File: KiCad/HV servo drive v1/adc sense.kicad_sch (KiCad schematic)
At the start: 38 parts, among them J6 PFC SENSE

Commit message: KiCad 8.0 update
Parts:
- renumbered C36 to C28, C28 to C29, C29 to C30, C30 to C33, C33 to C34, C34 to C35, C35 to C36, D9 to D10, D10 to D12, D12 to D13, D13 to D14, D14 to D15, D15 to D8, D8 to D9, R44 to R25, R45 to R26, R25 to R27, R26 to R28, R27 to R29, R28 to R30, R29 to R38, R30 to R39, R38 to R40, R39 to R41, R40 to R42, R41 to R43, R42 to R44, R43 to R45

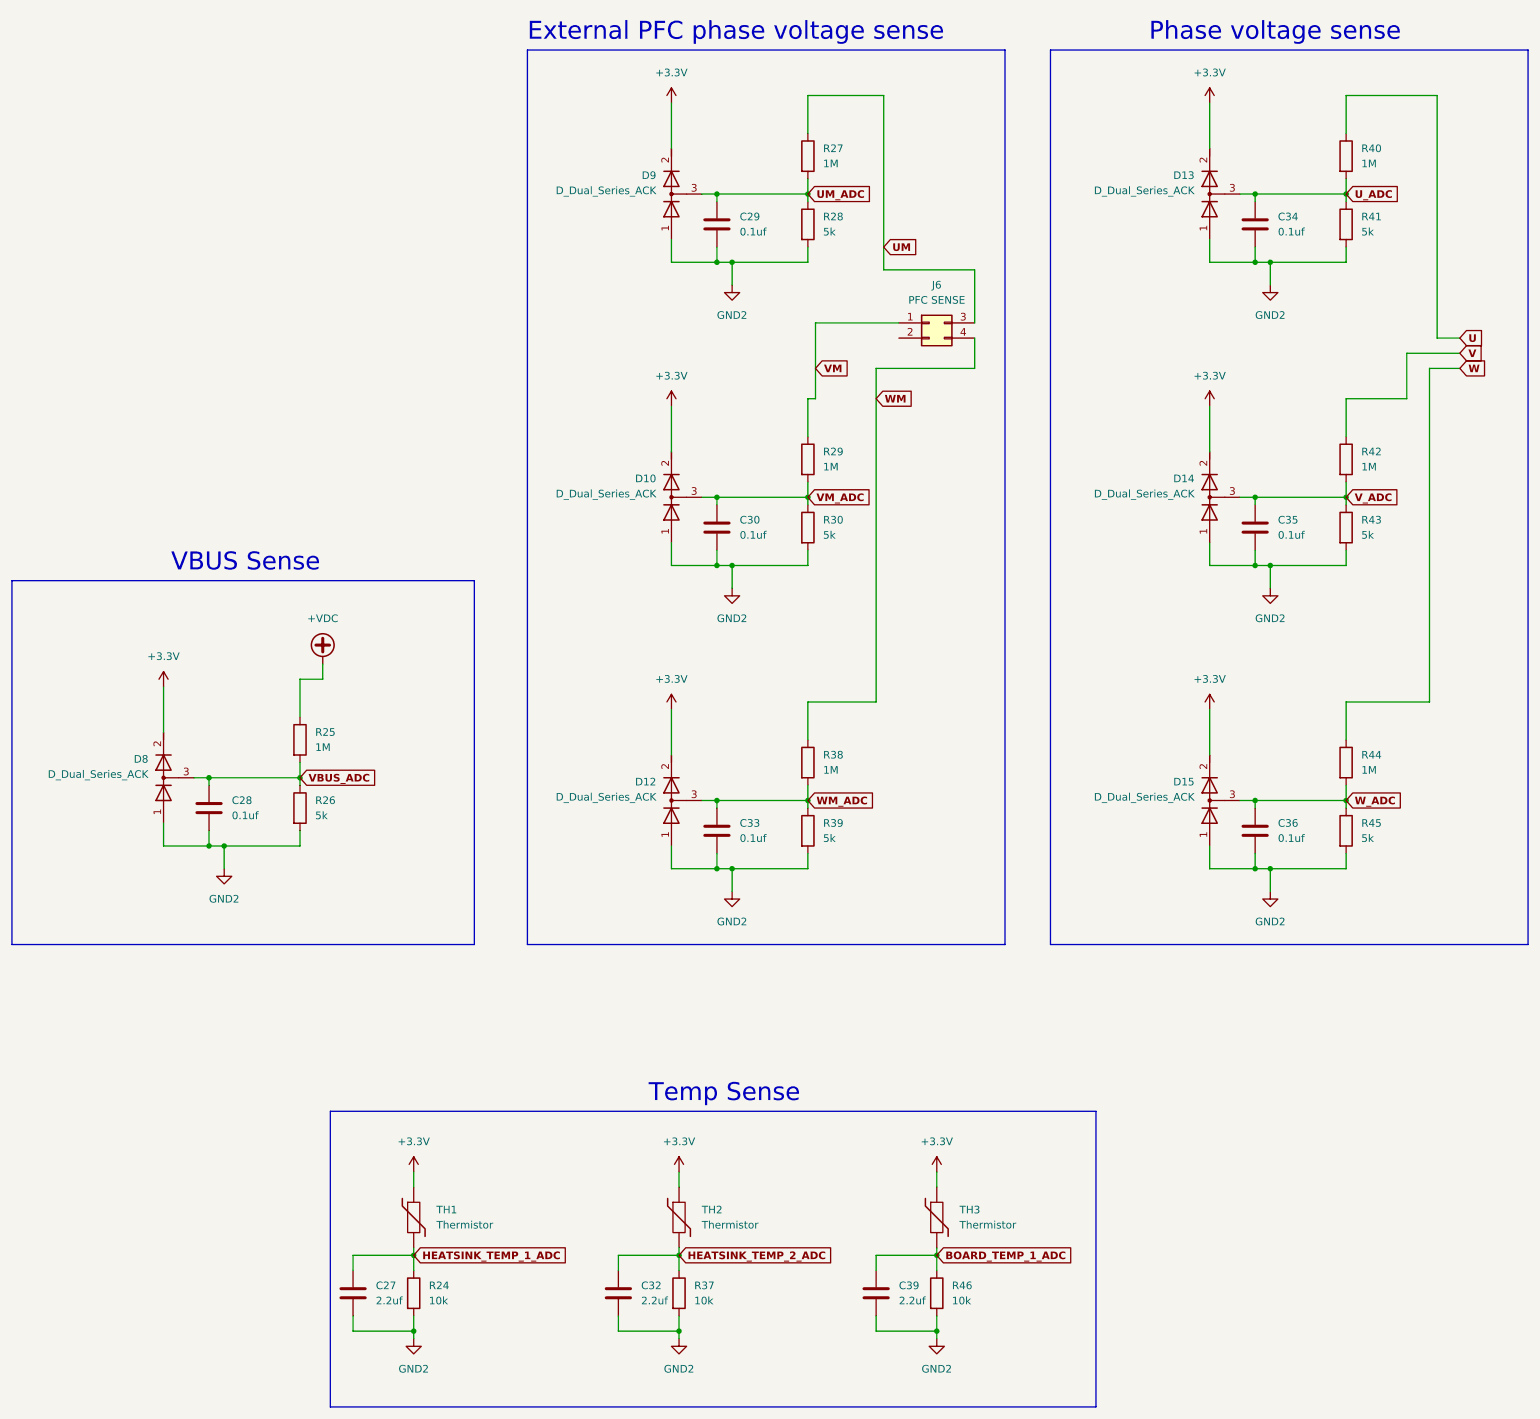
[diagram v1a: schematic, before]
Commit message: start rev 2 changes
fix component references, fix rj45 and dc-dc converter footprints, add RLC filters on all power connectors, add more mounting holes
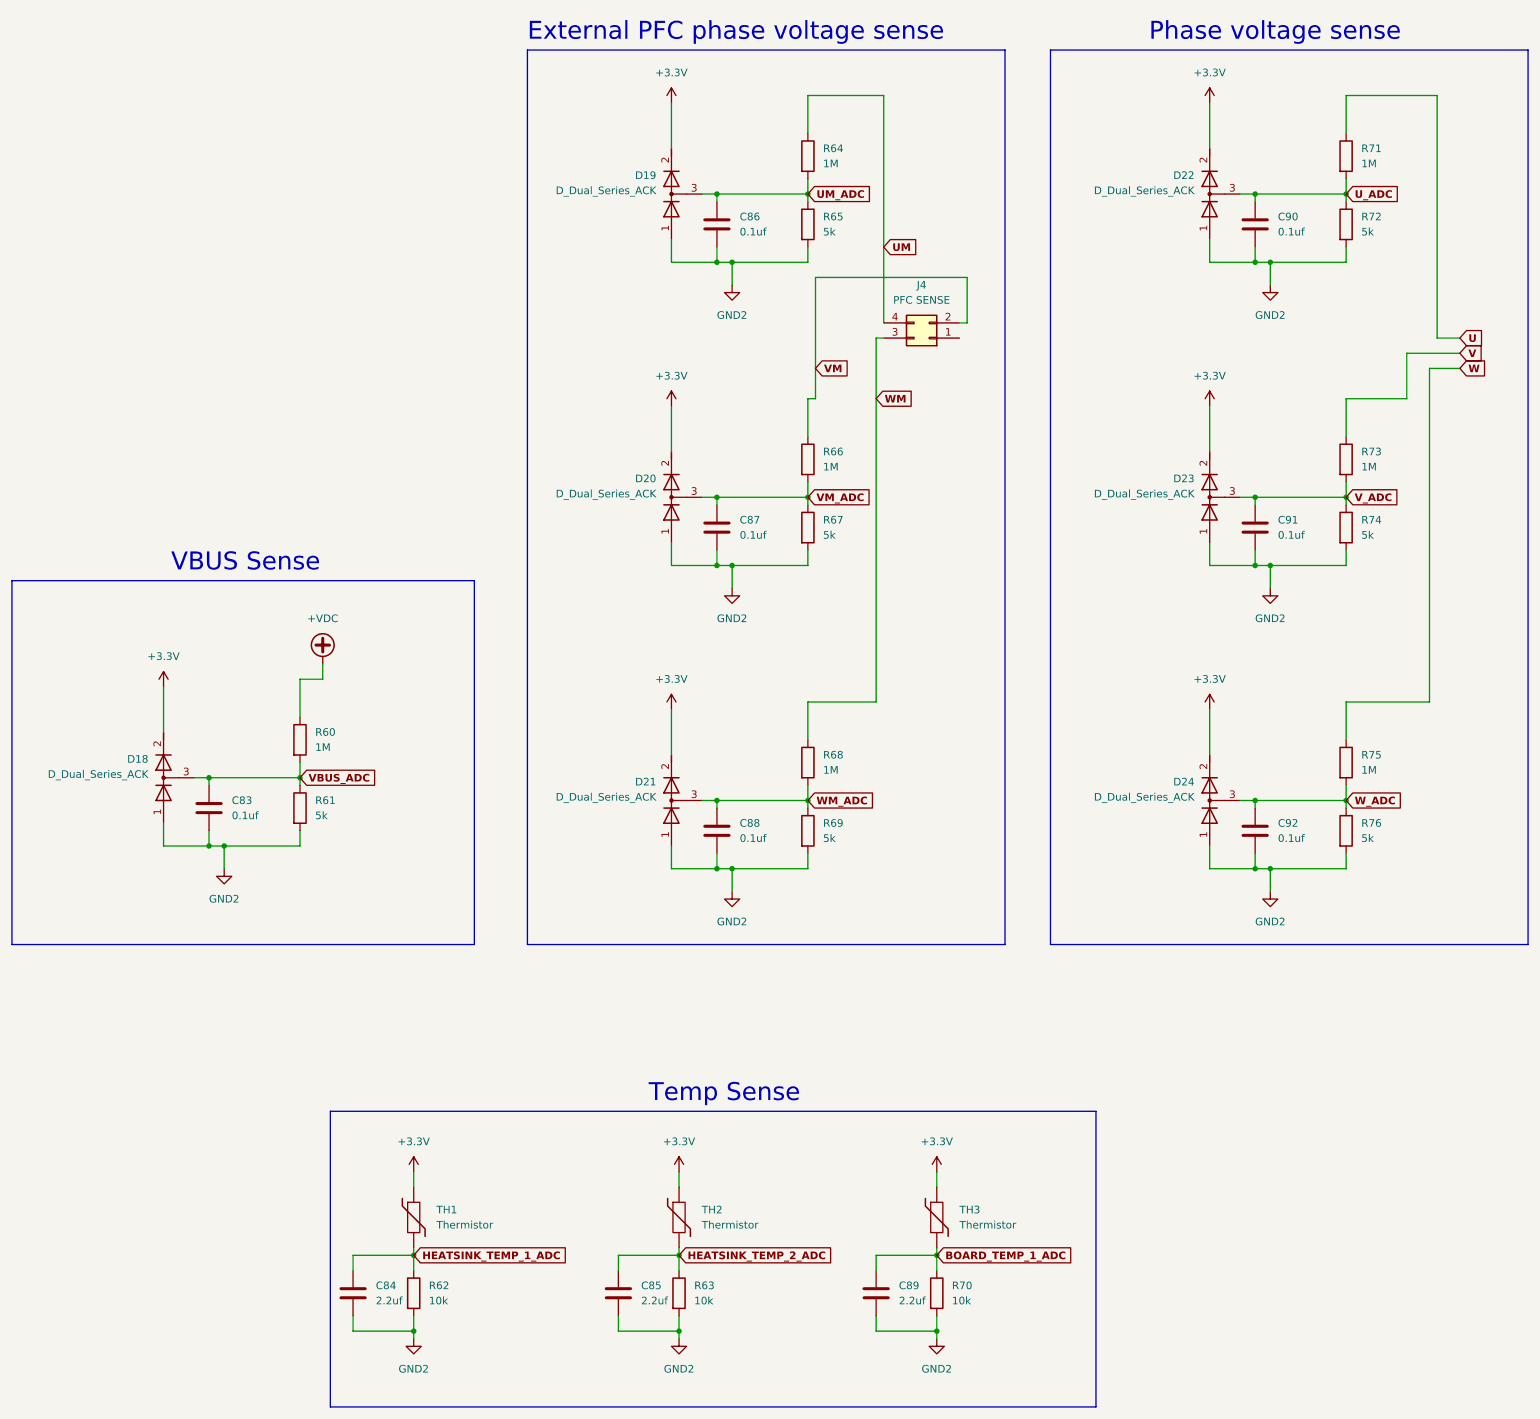
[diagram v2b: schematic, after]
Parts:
- renumbered C28 to C83, C27 to C84, C32 to C85, C29 to C86, C30 to C87, C33 to C88, C39 to C89, C34 to C90, C35 to C91, C36 to C92, D8 to D18, D9 to D19, D10 to D20, D12 to D21, D13 to D22, D14 to D23, D15 to D24, J6 to J4, R25 to R60, R26 to R61, R24 to R62, R37 to R63, R27 to R64, R28 to R65, R29 to R66, R30 to R67, R38 to R68, R39 to R69, R46 to R70, R40 to R71, R41 to R72, R42 to R73, R43 to R74, R44 to R75, R45 to R76
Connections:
- net UM: now also J4.4 (Pin_4); no longer J4.3 (Pin_3)
- net VM: now also J4.2 (Pin_2); no longer J4.1 (Pin_1)
- net WM: now also J4.3 (Pin_3); no longer J4.4 (Pin_4)
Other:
- moved on the sheet: J4

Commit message: update to rev 2.1
basically the same version as in the FOC youtube video, with some minor issues fixed
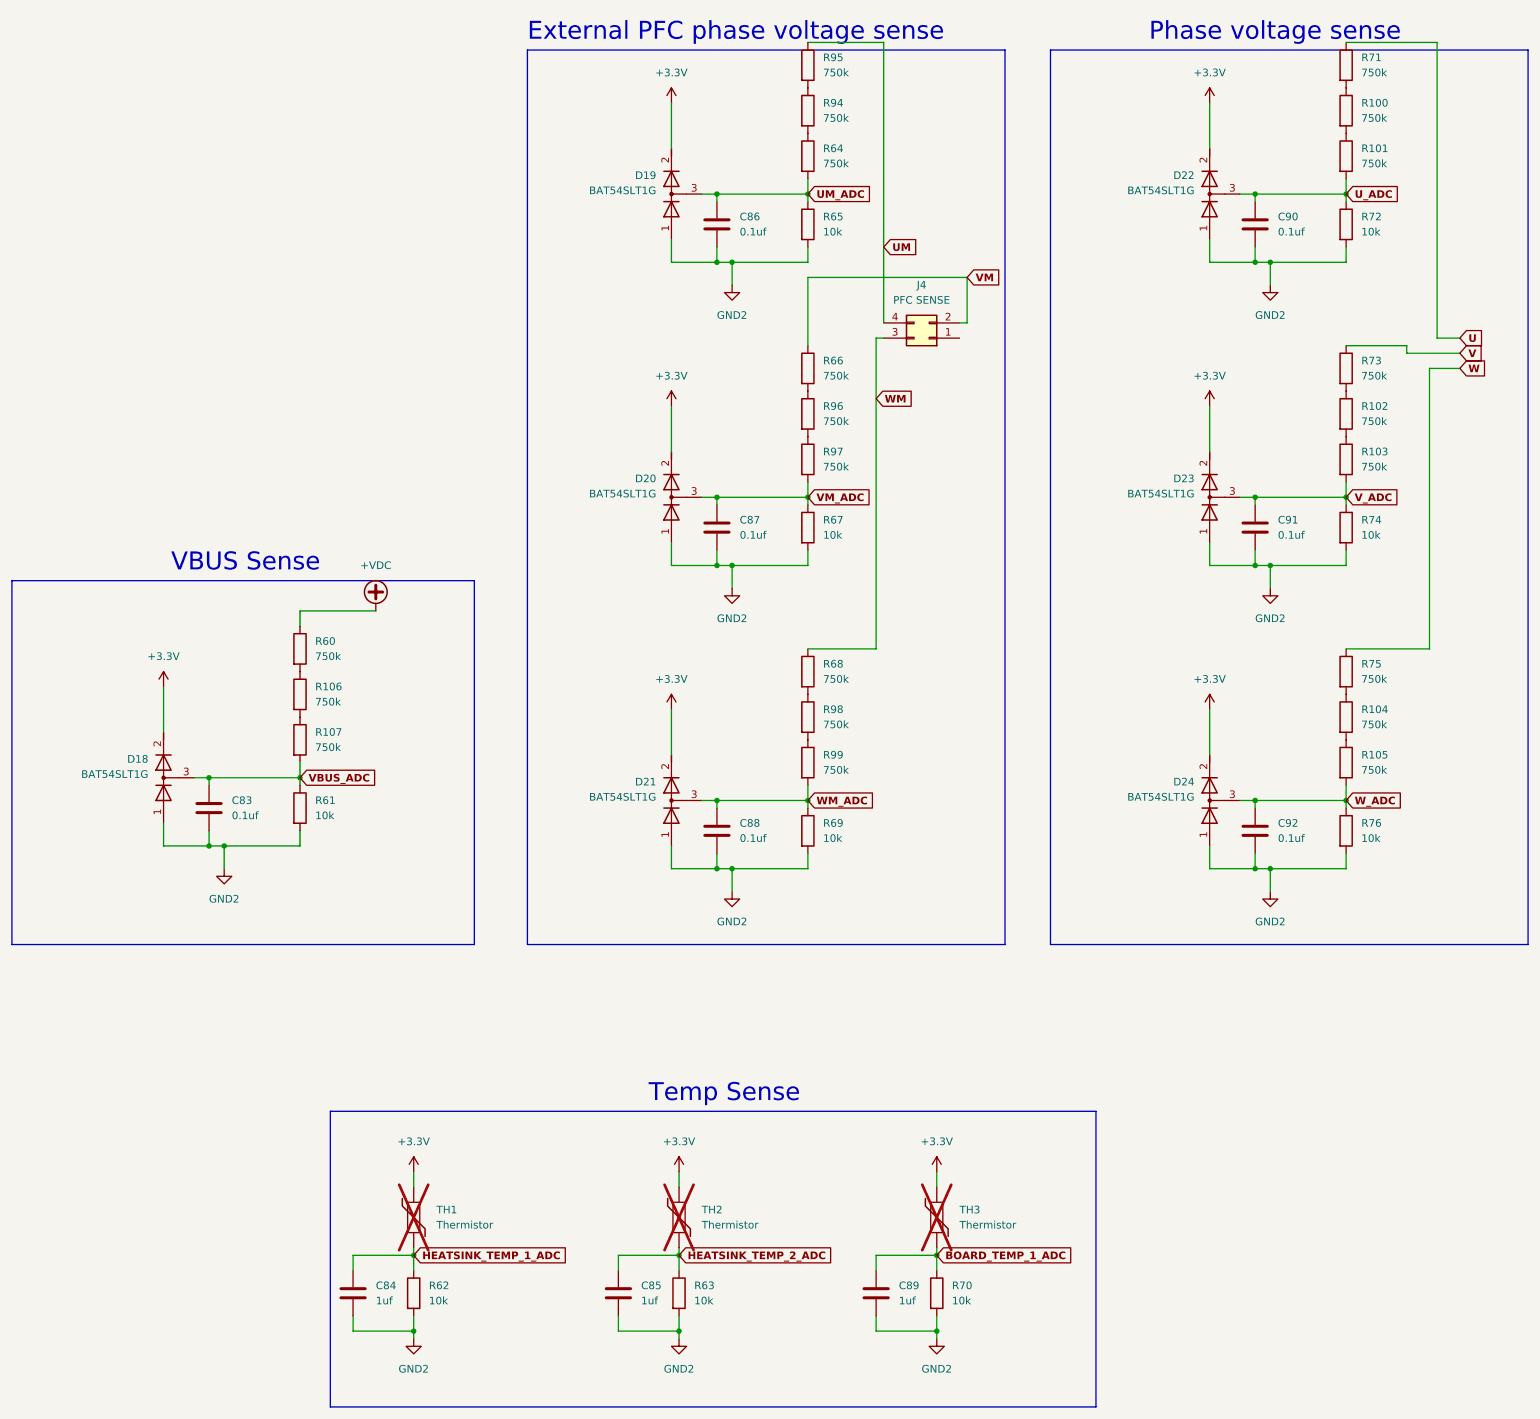
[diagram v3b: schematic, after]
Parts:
- added R100, R101, R102, R103, R104, R105, R106, R107, R94, R95, R96, R97, R98, R99: 750k, Resistor_SMD:R_1206_3216Metric, symbol Device:R
- C83, C86, C87, C88, C90, C91, C92: Generic Allowed? (none) -> yes; Manufacturer (none) -> YAGEO; Part number (none) -> CC0603ZRY5V9BB104
- C84, C85, C89: value 2.2uf -> 1uf; Generic Allowed? (none) -> yes; Manufacturer (none) -> Samsung Electro-Mechanics; Part number (none) -> CL10A105KB8NNNC
- D18, D19, D20, D21, D22, D23, D24: value D_Dual_Series_ACK -> BAT54SLT1G; Generic Allowed? (none) -> yes; Manufacturer (none) -> onsemi; Part number (none) -> BAT54SLT1G
- J4: Generic Allowed? (none) -> yes; Manufacturer (none) -> Molex; Part number (none) -> 0469990014
- R60, R64, R66, R68, R71, R73, R75: value 1M -> 750k; footprint Resistor_THT:R_Axial_DIN0309_L9.0mm_D3.2mm_P12.70mm_Horizontal -> Resistor_SMD:R_1206_3216Metric; Generic Allowed? (none) -> yes; Manufacturer (none) -> YAGEO; Part number (none) -> RC1206FR-07750KL
- R61, R65, R67, R69, R72, R74, R76: value 5k -> 10k; Generic Allowed? (none) -> yes; Manufacturer (none) -> YAGEO; Part number (none) -> RC0603FR-0710KL
- R62, R63, R70: Generic Allowed? (none) -> yes; Manufacturer (none) -> YAGEO; Part number (none) -> RC0603FR-0710KL
- TH1, TH2, TH3: now not fitted
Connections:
- net UM: now also R95.1; no longer R64.1
- net U_ADC: now also R101.2; no longer R71.2
- net VBUS_ADC: now also R107.2; no longer R60.2
- net VM_ADC: now also R97.2; no longer R66.2
- net V_ADC: now also R103.2; no longer R73.2
- net WM_ADC: now also R99.2; no longer R68.2
- net W_ADC: now also R105.2; no longer R75.2
- new net: R102.2, R103.1
- new net: R104.1, R75.2
- new net: R104.2, R105.1
- new net: R106.1, R60.2
- new net: R68.2, R98.1
- new net: R100.2, R101.1
- new net: R66.2, R96.1
- new net: R96.2, R97.1
- new net: R100.1, R71.2
- new net: R64.1, R94.2
- new net: R102.1, R73.2
- new net: R98.2, R99.1
- new net: R94.1, R95.2
- new net: R106.2, R107.1
